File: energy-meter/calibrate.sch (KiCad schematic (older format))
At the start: 20 parts, among them Q1 AP3400, U4 EPR211A354001EZ, U5 EPR211A354001EZ, U6 L9110S

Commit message: add opamps
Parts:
- removed D7: D_Schottky, Diode_SMD:D_SMA_Handsoldering, symbol Device:D_Schottky
- removed JP10: SolderJumper_2_Open, Jumper:SolderJumper-2_P1.3mm_Open_RoundedPad1.0x1.5mm, symbol Jumper:SolderJumper_2_Open
- removed JP9: SolderJumper_2_Bridged, Jumper:SolderJumper-2_P1.3mm_Bridged_RoundedPad1.0x1.5mm, symbol Jumper:SolderJumper_2_Bridged
- removed Q1: AP3400, Package_TO_SOT_SMD:SOT-23_Handsoldering, symbol Device:Q_NMOS_GSD
- removed R8: 10k, Resistor_SMD:R_0603_1608Metric_Pad1.05x0.95mm_HandSolder, symbol Device:R
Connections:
- net labels removed: RELAY2
- wire segments 51 -> 49
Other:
- note removed: "alternative use of the 2nd relay:\n- cut L_OUT around TP3\n- TP3 -> through T3 -> TP5\n- N -> TP4\n- L_OUT to external load, as usual\n=> K2 enables internal load"
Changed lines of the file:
@@
 Text GLabel 1250 900  2    50   Input ~ 0
 N
-Text Notes 8700 3900 0    50   ~ 0
-alternative use of the 2nd relay:\n- cut L_OUT around TP3\n- TP3 -> through T3 -> TP5\n- N -> TP4\n- L_OUT to external load, as usual\n=> K2 enables internal load
-$Comp
-L Device:Q_NMOS_GSD Q?
-U 1 1 61066D83
-P 9400 4550
-AR Path="/60846F2E/61066D83" Ref="Q?"  Part="1"
-AR Path="/60514CC5/61066D83" Ref="Q?"  Part="1"
-AR Path="/607B74C2/61066D83" Ref="Q?"  Part="1"
-AR Path="/61066D83" Ref="Q?"  Part="1"
-AR Path="/60F98E6C/61066D83" Ref="Q1"  Part="1"
-F 0 "Q1" H 9606 4596 50  0000 L CNN
-F 1 "AP3400" H 9606 4505 50  0000 L CNN
-F 2 "Package_TO_SOT_SMD:SOT-23_Handsoldering" H 9600 4650 50  0001 C CNN
-F 3 "https://datasheet.lcsc.com/szlcsc/1901071504_ShenZhen-Quan-Li-Semiconductor-AP3400_C353070.pdf" H 9400 4550 50  0001 C CNN
-F 4 "AP3400, C353070, HSS2306A, C518790, AO3400A, C700953" H 9400 4550 50  0001 C CNN "LCSC"
-	1    9400 4550
-	1    0    0    -1
-$EndComp
-$Comp
-L power:GND #PWR?
-U 1 1 61066D89
-P 9500 4750
-AR Path="/61066D89" Ref="#PWR?"  Part="1"
-AR Path="/60F98E6C/61066D89" Ref="#PWR0138"  Part="1"
-F 0 "#PWR0138" H 9500 4500 50  0001 C CNN
-F 1 "GND" V 9505 4622 50  0000 R CNN
-F 2 "" H 9500 4750 50  0001 C CNN
-F 3 "" H 9500 4750 50  0001 C CNN
-	1    9500 4750
-	1    0    0    -1
-$EndComp
-Wire Wire Line
-	9500 4100 9500 4350
-$Comp
-L Device:D_Schottky D?
-U 1 1 61066D91
-P 10150 4650
-AR Path="/61066D91" Ref="D?"  Part="1"
-AR Path="/60F98E6C/61066D91" Ref="D7"  Part="1"
-F 0 "D7" V 10150 4500 50  0000 L CNN
-F 1 "D_Schottky" H 10150 4775 50  0001 C CNN
-F 2 "Diode_SMD:D_SMA_Handsoldering" H 10150 4650 50  0001 C CNN
-F 3 "~" H 10150 4650 50  0001 C CNN
-F 4 "C181203, C364270, C50645" H 10150 4650 50  0001 C CNN "LCSC"
-	1    10150 4650
-	0    -1   -1   0
-$EndComp
-Text Label 9200 4550 1    50   ~ 0
-RELAY2
-$Comp
-L Device:R R?
-U 1 1 61066D98
-P 9200 4800
-AR Path="/602A3FC4/61066D98" Ref="R?"  Part="1"
-AR Path="/60514CC5/61066D98" Ref="R?"  Part="1"
-AR Path="/607B74C2/61066D98" Ref="R?"  Part="1"
-AR Path="/61066D98" Ref="R?"  Part="1"
-AR Path="/60F98E6C/61066D98" Ref="R8"  Part="1"
-F 0 "R8" V 8993 4800 50  0000 C CNN
-F 1 "10k" V 9084 4800 50  0000 C CNN
-F 2 "Resistor_SMD:R_0603_1608Metric_Pad1.05x0.95mm_HandSolder" V 9130 4800 50  0001 C CNN
-F 3 "~" H 9200 4800 50  0001 C CNN
-	1    9200 4800
-	-1   0    0    1
-$EndComp
-$Comp
-L power:GND #PWR?
-U 1 1 61066D9E
-P 9200 4950
-AR Path="/61066D9E" Ref="#PWR?"  Part="1"
-AR Path="/60F98E6C/61066D9E" Ref="#PWR0139"  Part="1"
-F 0 "#PWR0139" H 9200 4700 50  0001 C CNN
-F 1 "GND" V 9205 4822 50  0000 R CNN
-F 2 "" H 9200 4950 50  0001 C CNN
-F 3 "" H 9200 4950 50  0001 C CNN
-	1    9200 4950
-	1    0    0    -1
-$EndComp
-Wire Wire Line
-	9200 4650 9200 4550
 $Comp
 L Device:R R?
@@
 	1    2100 2450
 	1    0    0    -1
-$EndComp
-$Comp
-L Jumper:SolderJumper_2_Open JP?
-U 1 1 610BEE8F
-P 8500 5350
-AR Path="/610BEE8F" Ref="JP?"  Part="1"
-AR Path="/60F98E6C/610BEE8F" Ref="JP10"  Part="1"
-F 0 "JP10" V 8500 5418 50  0000 L CNN
-F 1 "SolderJumper_2_Open" H 8500 5464 50  0001 C CNN
-F 2 "Jumper:SolderJumper-2_P1.3mm_Open_RoundedPad1.0x1.5mm" H 8500 5350 50  0001 C CNN
-F 3 "~" H 8500 5350 50  0001 C CNN
-	1    8500 5350
-	0    1    1    0
 $EndComp
 $Comp
@@
 	1    0    0    -1
 $EndComp
-$Comp
-L Jumper:SolderJumper_2_Bridged JP?
-U 1 1 610BEE7D
-P 8500 4900
-AR Path="/610BEE7D" Ref="JP?"  Part="1"
-AR Path="/60F98E6C/610BEE7D" Ref="JP9"  Part="1"
-F 0 "JP9" V 8500 4968 50  0000 L CNN
-F 1 "SolderJumper_2_Bridged" H 8500 5014 50  0001 C CNN
-F 2 "Jumper:SolderJumper-2_P1.3mm_Bridged_RoundedPad1.0x1.5mm" H 8500 4900 50  0001 C CNN
-F 3 "~" H 8500 4900 50  0001 C CNN
-	1    8500 4900
-	0    1    1    0
-$EndComp
-Wire Wire Line
+Wire Wire Line

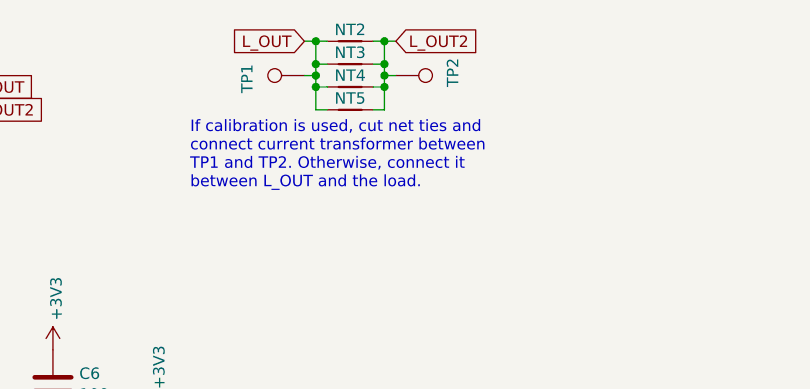
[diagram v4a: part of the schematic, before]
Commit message: remove optional parts, increase distance between conductors on primary side
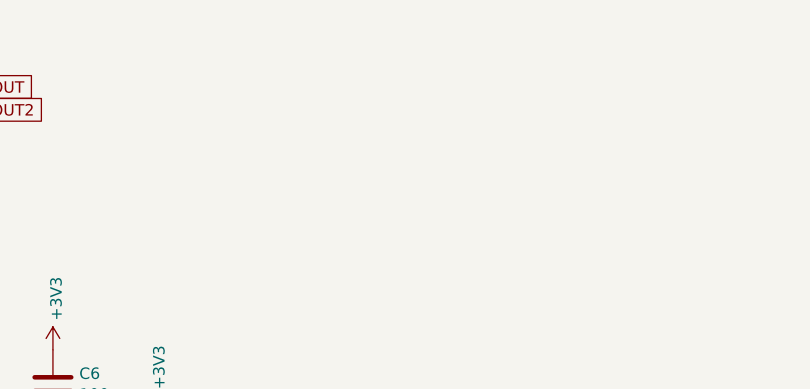
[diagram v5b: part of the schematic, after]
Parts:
- removed NT2, NT3, NT4, NT5: Net-Tie_2, NetTie:NetTie-2_SMD_Pad2.0mm, symbol Device:Net-Tie_2
- removed TP1, TP2: TestPoint, TestPoint:TestPoint_THTPad_D3.0mm_Drill1.5mm, symbol Connector:TestPoint
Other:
- note removed: "If calibration is used, cut net ties and\nconnect current transformer between\nTP1 and TP2. Otherwise, connect it\nbetween L_OUT and the load."
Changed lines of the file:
@@
 Comment4 ""
 $EndDescr
-$Comp
-L Connector:TestPoint TP?
-U 1 1 61044130
-P 2750 950
-AR Path="/61044130" Ref="TP?"  Part="1"
-AR Path="/60F98E6C/61044130" Ref="TP1"  Part="1"
-F 0 "TP1" H 2800 1200 50  0000 R CNN
-F 1 "TestPoint" H 2808 977 50  0001 L CNN
-F 2 "TestPoint:TestPoint_THTPad_D3.0mm_Drill1.5mm" H 2950 950 50  0001 C CNN
-F 3 "~" H 2950 950 50  0001 C CNN
-	1    2750 950
-	0    -1   -1   0
-$EndComp
-$Comp
-L Connector:TestPoint TP?
-U 1 1 61044136
-P 3150 950
-AR Path="/61044136" Ref="TP?"  Part="1"
-AR Path="/60F98E6C/61044136" Ref="TP2"  Part="1"
-F 0 "TP2" H 3200 1200 50  0000 R CNN
-F 1 "TestPoint" H 3208 977 50  0001 L CNN
-F 2 "TestPoint:TestPoint_THTPad_D3.0mm_Drill1.5mm" H 3350 950 50  0001 C CNN
-F 3 "~" H 3350 950 50  0001 C CNN
-	1    3150 950
-	0    1    1    0
-$EndComp
-Text GLabel 3150 800  2    50   Input ~ 0
-L_OUT2
-Text GLabel 2750 800  0    50   Input ~ 0
-L_OUT
-$Comp
-L Device:Net-Tie_2 NT?
-U 1 1 6104413E
-P 2950 800
-AR Path="/6104413E" Ref="NT?"  Part="1"
-AR Path="/60F98E6C/6104413E" Ref="NT2"  Part="1"
-F 0 "NT2" H 2950 750 50  0000 C CNN
-F 1 "Net-Tie_2" H 2950 890 50  0001 C CNN
-F 2 "NetTie:NetTie-2_SMD_Pad2.0mm" H 2950 800 50  0001 C CNN
-F 3 "~" H 2950 800 50  0001 C CNN
-	1    2950 800
-	-1   0    0    1
-$EndComp
-$Comp
-L Device:Net-Tie_2 NT?
-U 1 1 61044144
-P 2950 900
-AR Path="/61044144" Ref="NT?"  Part="1"
-AR Path="/60F98E6C/61044144" Ref="NT3"  Part="1"
-F 0 "NT3" H 2950 850 50  0000 C CNN
-F 1 "Net-Tie_2" H 2950 990 50  0001 C CNN
-F 2 "NetTie:NetTie-2_SMD_Pad2.0mm" H 2950 900 50  0001 C CNN
-F 3 "~" H 2950 900 50  0001 C CNN
-	1    2950 900
-	-1   0    0    1
-$EndComp
-$Comp
-L Device:Net-Tie_2 NT?
-U 1 1 6104414A
-P 2950 1000
-AR Path="/6104414A" Ref="NT?"  Part="1"
-AR Path="/60F98E6C/6104414A" Ref="NT4"  Part="1"
-F 0 "NT4" H 2950 950 50  0000 C CNN
-F 1 "Net-Tie_2" H 2950 1090 50  0001 C CNN
-F 2 "NetTie:NetTie-2_SMD_Pad2.0mm" H 2950 1000 50  0001 C CNN
-F 3 "~" H 2950 1000 50  0001 C CNN
-	1    2950 1000
-	-1   0    0    1
-$EndComp
-Wire Wire Line
-	2750 800  2800 800
-Wire Wire Line
-	2800 800  2800 900
-Wire Wire Line
-	2800 1000 2850 1000
-Connection ~ 2800 800
-Wire Wire Line
-	2800 800  2850 800
-Wire Wire Line
-	2800 950  2750 950
-Connection ~ 2800 950
-Wire Wire Line
-	2800 950  2800 1000
-Wire Wire Line
-	2850 900  2800 900
-Connection ~ 2800 900
-Wire Wire Line
-	2800 900  2800 950
-Wire Wire Line
-	3050 800  3100 800
-Wire Wire Line
-	3100 800  3100 900
-Wire Wire Line
-	3100 1000 3050 1000
-Connection ~ 3100 800
-Wire Wire Line
-	3100 800  3150 800
-Wire Wire Line
-	3150 950  3100 950
-Connection ~ 3100 950
-Wire Wire Line
-	3100 950  3100 1000
-Wire Wire Line
-	3050 900  3100 900
-Connection ~ 3100 900
-Wire Wire Line
-	3100 900  3100 950
-Text Notes 2250 1450 0    50   ~ 0
-If calibration is used, cut net ties and\nconnect current transformer between\nTP1 and TP2. Otherwise, connect it\nbetween L_OUT and the load.
-$Comp
-L Device:Net-Tie_2 NT?
-U 1 1 61044167
-P 2950 1100
-AR Path="/61044167" Ref="NT?"  Part="1"
-AR Path="/60F98E6C/61044167" Ref="NT5"  Part="1"
-F 0 "NT5" H 2950 1050 50  0000 C CNN
-F 1 "Net-Tie_2" H 2950 1190 50  0001 C CNN
-F 2 "NetTie:NetTie-2_SMD_Pad2.0mm" H 2950 1100 50  0001 C CNN
-F 3 "~" H 2950 1100 50  0001 C CNN
-	1    2950 1100
-	-1   0    0    1
-$EndComp
-Wire Wire Line
-	3050 1100 3100 1100
-Wire Wire Line
-	3100 1100 3100 1000
-Connection ~ 3100 1000
-Wire Wire Line
-	2800 1100 2800 1000
-Connection ~ 2800 1000
-Wire Wire Line
-	2850 1100 2800 1100
 Text HLabel 1250 900  0    50   Input ~ 0
 N

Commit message: increase size of test points for wire through current transformer, unswap RELAY_SET/RESET
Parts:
- added TP1, TP2: TestPoint, TestPoint:TestPoint_THTPad_D4.0mm_Drill2.0mm, symbol Connector:TestPoint
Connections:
- net L_OUT: now also TP1.1
- net L_OUT2: now also TP2.1
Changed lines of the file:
@@
 Text HLabel 1150 3250 0    50   Input ~ 0
 ENA_470k
+Wire Wire Line
+	3150 950  3100 950
+Wire Wire Line
+	3100 800  3150 800
+Wire Wire Line
+	2800 950  2750 950
+Wire Wire Line
+	2750 800  2800 800
+Text GLabel 2750 800  0    50   Input ~ 0
+L_OUT
+Text GLabel 3150 800  2    50   Input ~ 0
+L_OUT2
+$Comp
+L Connector:TestPoint TP?
+U 1 1 61044136
+P 3150 950
+AR Path="/61044136" Ref="TP?"  Part="1"
+AR Path="/60F98E6C/61044136" Ref="TP2"  Part="1"
+F 0 "TP2" H 3200 1200 50  0000 R CNN
+F 1 "TestPoint" H 3208 977 50  0001 L CNN
+F 2 "TestPoint:TestPoint_THTPad_D4.0mm_Drill2.0mm" H 3350 950 50  0001 C CNN
+F 3 "~" H 3350 950 50  0001 C CNN
+	1    3150 950
+	0    1    1    0
+$EndComp
+$Comp
+L Connector:TestPoint TP?
+U 1 1 61044130
+P 2750 950
+AR Path="/61044130" Ref="TP?"  Part="1"
+AR Path="/60F98E6C/61044130" Ref="TP1"  Part="1"
+F 0 "TP1" H 2800 1200 50  0000 R CNN
+F 1 "TestPoint" H 2808 977 50  0001 L CNN
+F 2 "TestPoint:TestPoint_THTPad_D4.0mm_Drill2.0mm" H 2950 950 50  0001 C CNN
+F 3 "~" H 2950 950 50  0001 C CNN
+	1    2750 950
+	0    -1   -1   0
+$EndComp
+Wire Wire Line
+	2800 800  2800 950
+Wire Wire Line
+	3100 800  3100 950
 $EndSCHEMATC
